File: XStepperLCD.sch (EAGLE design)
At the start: 43 parts, among them Q2 16 MHZ, U1 LCD-16X2NOHOLES

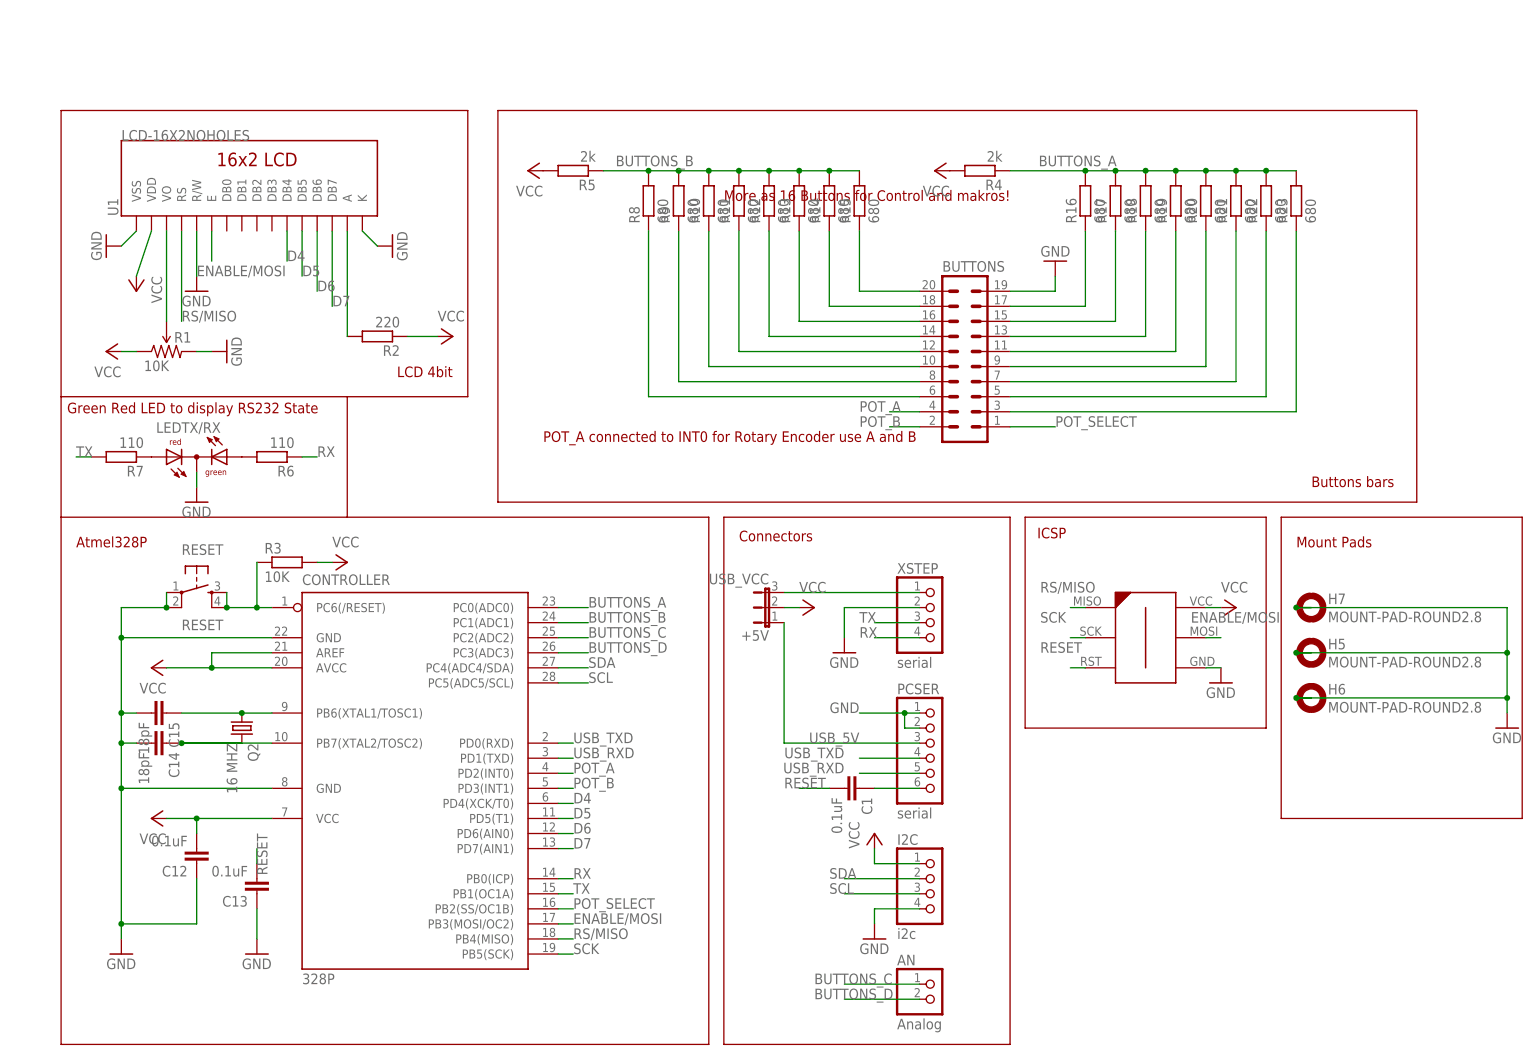
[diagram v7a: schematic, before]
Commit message: - get button values only from A0
- stop/restart all threads in get values command
- refresh silkscreen in board and design
- set version 0.2 in code
- remove some comments
- add group init for threads
- reformat code
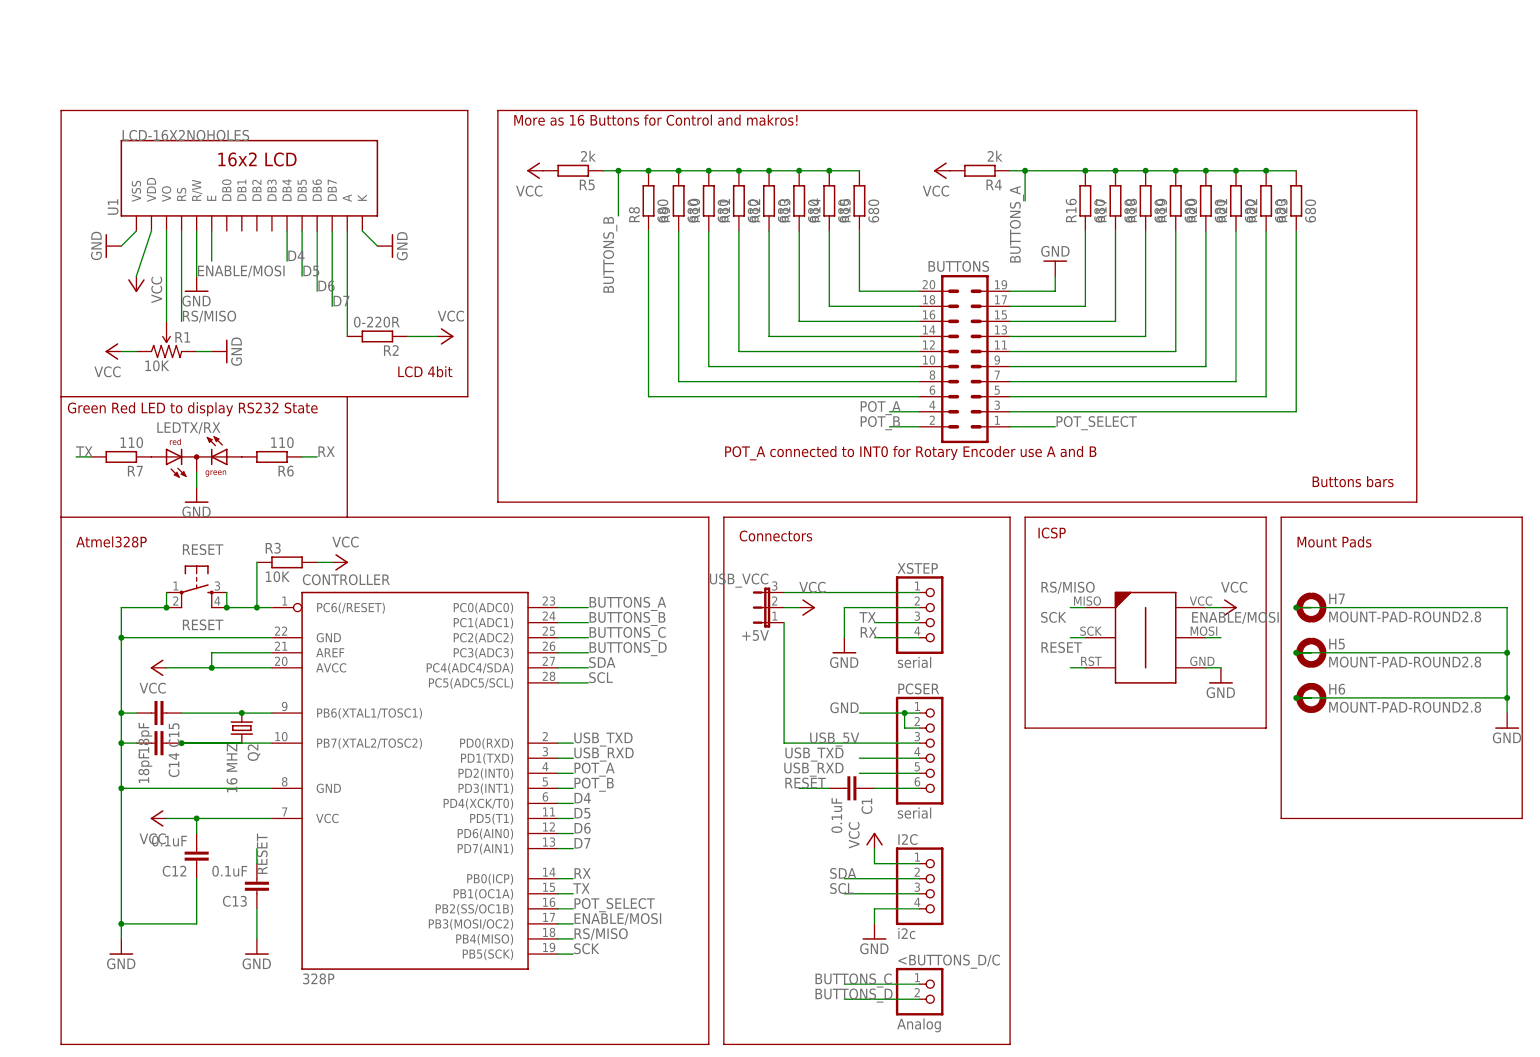
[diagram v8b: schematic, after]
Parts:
- R2: value 220 -> 0-220R
- renumbered AN to <BUTTONS_D/C
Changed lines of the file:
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@@
 <?xml version="1.0" encoding="utf-8"?>
 <!DOCTYPE eagle SYSTEM "eagle.dtd">
-<eagle version="6.4">
+<eagle version="6.5.0">
 <drawing>
 <settings>
@@
 <grid distance="0.1" unitdist="inch" unit="inch" style="lines" multiple="1" display="no" altdistance="0.01" altunitdist="inch" altunit="inch"/>
 <layers>
-<layer number="1" name="Top" color="4" fill="1" visible="yes" active="no"/>
-<layer number="16" name="Bottom" color="1" fill="1" visible="yes" active="no"/>
-<layer number="17" name="Pads" color="2" fill="1" visible="yes" active="no"/>
-<layer number="18" name="Vias" color="2" fill="1" visible="yes" active="no"/>
-<layer number="19" name="Unrouted" color="6" fill="1" visible="yes" active="no"/>
-<layer number="20" name="Dimension" color="15" fill="1" visible="yes" active="no"/>
-<layer number="21" name="tPlace" color="7" fill="1" visible="yes" active="no"/>
-<layer number="22" name="bPlace" color="7" fill="1" visible="yes" active="no"/>
-<layer number="23" name="tOrigins" color="15" fill="1" visible="yes" active="no"/>
-<layer number="24" name="bOrigins" color="15" fill="1" visible="yes" active="no"/>
-<layer number="25" name="tNames" color="7" fill="1" visible="yes" active="no"/>
-<layer number="26" name="bNames" color="7" fill="1" visible="yes" active="no"/>
-<layer number="27" name="tValues" color="7" fill="1" visible="yes" active="no"/>
-<layer number="28" name="bValues" color="7" fill="1" visible="yes" active="no"/>
+<layer number="1" name="Top" color="4" fill="1" visible="no" active="no"/>
+<layer number="16" name="Bottom" color="1" fill="1" visible="no" active="no"/>
+<layer number="17" name="Pads" color="2" fill="1" visible="no" active="no"/>
+<layer number="18" name="Vias" color="2" fill="1" visible="no" active="no"/>
+<layer number="19" name="Unrouted" color="6" fill="1" visible="no" active="no"/>
+<layer number="20" name="Dimension" color="15" fill="1" visible="no" active="no"/>
+<layer number="21" name="tPlace" color="7" fill="1" visible="no" active="no"/>
+<layer number="22" name="bPlace" color="7" fill="1" visible="no" active="no"/>
+<layer number="23" name="tOrigins" color="15" fill="1" visible="no" active="no"/>
+<layer number="24" name="bOrigins" color="15" fill="1" visible="no" active="no"/>
+<layer number="25" name="tNames" color="7" fill="1" visible="no" active="no"/>
+<layer number="26" name="bNames" color="7" fill="1" visible="no" active="no"/>
+<layer number="27" name="tValues" color="7" fill="1" visible="no" active="no"/>
+<layer number="28" name="bValues" color="7" fill="1" visible="no" active="no"/>
 <layer number="29" name="tStop" color="7" fill="3" visible="no" active="no"/>
 <layer number="30" name="bStop" color="7" fill="6" visible="no" active="no"/>
@@
 <layer number="35" name="tGlue" color="7" fill="4" visible="no" active="no"/>
 <layer number="36" name="bGlue" color="7" fill="5" visible="no" active="no"/>
-<layer number="37" name="tTest" color="7" fill="1" visible="yes" active="no"/>
-<layer number="38" name="bTest" color="7" fill="1" visible="yes" active="no"/>
+<layer number="37" name="tTest" color="7" fill="1" visible="no" active="no"/>
+<layer number="38" name="bTest" color="7" fill="1" visible="no" active="no"/>
 <layer number="39" name="tKeepout" color="4" fill="11" visible="no" active="no"/>
 <layer number="40" name="bKeepout" color="1" fill="11" visible="no" active="no"/>
@@
 <layer number="44" name="Drills" color="7" fill="1" visible="no" active="no"/>
 <layer number="45" name="Holes" color="7" fill="1" visible="no" active="no"/>
-<layer number="46" name="Milling" color="3" fill="1" visible="yes" active="no"/>
-<layer number="47" name="Measures" color="7" fill="1" visible="yes" active="no"/>
-<layer number="48" name="Document" color="7" fill="1" visible="yes" active="no"/>
-<layer number="49" name="Reference" color="7" fill="1" visible="yes" active="no"/>
-<layer number="50" name="dxf" color="7" fill="1" visible="yes" active="no"/>
-<layer number="51" name="tDocu" color="7" fill="1" visible="yes" active="no"/>
-<layer number="52" name="bDocu" color="7" fill="1" visible="yes" active="no"/>
-<layer number="53" name="tGND_GNDA" color="7" fill="9" visible="yes" active="no"/>
-<layer number="54" name="bGND_GNDA" color="1" fill="9" visible="yes" active="no"/>
-<layer number="56" name="wert" color="7" fill="1" visible="yes" active="no"/>
+<layer number="46" name="Milling" color="3" fill="1" visible="no" active="no"/>
+<layer number="47" name="Measures" color="7" fill="1" visible="no" active="no"/>
+<layer number="48" name="Document" color="7" fill="1" visible="no" active="no"/>
+<layer number="49" name="Reference" color="7" fill="1" visible="no" active="no"/>
+<layer number="50" name="dxf" color="7" fill="1" visible="no" active="no"/>
+<layer number="51" name="tDocu" color="7" fill="1" visible="no" active="no"/>
+<layer number="52" name="bDocu" color="7" fill="1" visible="no" active="no"/>
+<layer number="53" name="tGND_GNDA" color="7" fill="9" visible="no" active="no"/>
+<layer number="54" name="bGND_GNDA" color="1" fill="9" visible="no" active="no"/>
+<layer number="56" name="wert" color="7" fill="1" visible="no" active="no"/>
 <layer number="91" name="Nets" color="2" fill="1" visible="yes" active="yes"/>
 <layer number="92" name="Busses" color="1" fill="1" visible="yes" active="yes"/>
@@
 <part name="P+6" library="supply1" deviceset="VCC" device=""/>
 <part name="GND1" library="supply1" deviceset="GND" device=""/>
-<part name="R2" library="resistor" deviceset="R-EU_" device="R1206" value="220"/>
+<part name="R2" library="resistor" deviceset="R-EU_" device="R1206" value="0-220R"/>
 <part name="P+1" library="supply1" deviceset="VCC" device=""/>
 <part name="BUTTONS" library="con-ml" deviceset="ML20" device=""/>
@@
 <part name="R22" library="resistor" deviceset="R-EU_" device="R1206" value="680"/>
 <part name="R23" library="resistor" deviceset="R-EU_" device="R1206" value="680"/>
-<part name="AN" library="pinhead" deviceset="PINHD-1X2" device="" value="Analog"/>
+<part name="&lt;BUTTONS_D/C" library="pinhead" deviceset="PINHD-1X2" device="" value="Analog"/>
 </parts>
 <sheets>
@@
 <text x="-1.524" y="55.626" size="1.778" layer="94">Green Red LED to display RS232 State</text>
 <text x="63.5" y="63.5" size="1.778" layer="94" rot="R180">LCD 4bit</text>
-<text x="78.74" y="50.8" size="1.778" layer="94">POT_A connected to INT0 for Rotary Encoder use A and B</text>
-<text x="109.22" y="91.44" size="1.778" layer="94">More as 16 Buttons for Control and makros!</text>
+<text x="109.22" y="48.26" size="1.778" layer="94">POT_A connected to INT0 for Rotary Encoder use A and B</text>
+<text x="73.66" y="104.14" size="1.778" layer="94">More as 16 Buttons for Control and makros!</text>
 </plain>
 <instances>
@@
 <instance part="R2" gate="G$1" x="50.8" y="68.58" rot="R180"/>
 <instance part="P+1" gate="VCC" x="63.5" y="68.58" rot="R270"/>
-<instance part="BUTTONS" gate="1" x="149.86" y="66.04"/>
+<instance part="BUTTONS" gate="1" x="149.86" y="66.04" smashed="yes">
+<attribute name="VALUE" x="146.05" y="48.26" size="1.778" layer="96"/>
+<attribute name="NAME" x="143.51" y="79.502" size="1.778" layer="95"/>
+</instance>
 <instance part="P+9" gate="VCC" x="144.78" y="96.52" rot="R90"/>
 <instance part="R4" gate="G$1" x="152.4" y="96.52" rot="R180"/>
@@
 <instance part="R22" gate="G$1" x="200.66" y="91.44" rot="R90"/>
 <instance part="R23" gate="G$1" x="205.74" y="91.44" rot="R90"/>
-<instance part="AN" gate="G$1" x="144.78" y="-43.18"/>
+<instance part="&lt;BUTTONS_D/C" gate="G$1" x="144.78" y="-43.18"/>
 </instances>
 <busses>
@@
 <pinref part="R4" gate="G$1" pin="1"/>
 <pinref part="R16" gate="G$1" pin="2"/>
-<wire x1="157.48" y1="96.52" x2="170.18" y2="96.52" width="0.1524" layer="91"/>
+<wire x1="157.48" y1="96.52" x2="160.02" y2="96.52" width="0.1524" layer="91"/>
 <pinref part="R17" gate="G$1" pin="2"/>
+<wire x1="160.02" y1="96.52" x2="170.18" y2="96.52" width="0.1524" layer="91"/>
 <wire x1="170.18" y1="96.52" x2="175.26" y2="96.52" width="0.1524" layer="91"/>
 <junction x="170.18" y="96.52"/>
@@
 <wire x1="200.66" y1="96.52" x2="205.74" y2="96.52" width="0.1524" layer="91"/>
 <junction x="200.66" y="96.52"/>
-<label x="162.306" y="97.282" size="1.778" layer="95"/>
+<wire x1="160.02" y1="96.52" x2="160.02" y2="91.44" width="0.1524" layer="91"/>
+<junction x="160.02" y="96.52"/>
+<label x="157.48" y="93.98" size="1.778" layer="95" rot="R270"/>
 </segment>
 </net>
@@
 </segment>
 <segment>
-<label x="104.14" y="99.06" size="1.778" layer="95" rot="R180"/>
 <pinref part="R9" gate="G$1" pin="2"/>
 <pinref part="R10" gate="G$1" pin="2"/>
@@
 <pinref part="R5" gate="G$1" pin="1"/>
 <pinref part="R8" gate="G$1" pin="2"/>
-<wire x1="88.9" y1="96.52" x2="96.52" y2="96.52" width="0.1524" layer="91"/>
+<wire x1="88.9" y1="96.52" x2="91.44" y2="96.52" width="0.1524" layer="91"/>
+<wire x1="91.44" y1="96.52" x2="96.52" y2="96.52" width="0.1524" layer="91"/>
 <wire x1="96.52" y1="96.52" x2="101.6" y2="96.52" width="0.1524" layer="91"/>
 <junction x="96.52" y="96.52"/>
 <junction x="101.6" y="96.52"/>
+<wire x1="91.44" y1="96.52" x2="91.44" y2="88.9" width="0.1524" layer="91"/>
+<junction x="91.44" y="96.52"/>
+<label x="88.9" y="88.9" size="1.778" layer="95" rot="R270"/>
 </segment>
 </net>
@@
 </segment>
 <segment>
-<pinref part="AN" gate="G$1" pin="1"/>
+<pinref part="&lt;BUTTONS_D/C" gate="G$1" pin="1"/>
 <wire x1="142.24" y1="-40.64" x2="129.54" y2="-40.64" width="0.1524" layer="91"/>
 <label x="124.46" y="-40.64" size="1.778" layer="95"/>
@@
 </segment>
 <segment>
-<pinref part="AN" gate="G$1" pin="2"/>
+<pinref part="&lt;BUTTONS_D/C" gate="G$1" pin="2"/>
 <wire x1="142.24" y1="-43.18" x2="129.54" y2="-43.18" width="0.1524" layer="91"/>
 <label x="124.46" y="-43.18" size="1.778" layer="95"/>
